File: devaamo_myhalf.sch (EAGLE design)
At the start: 18 parts, among them X1 PIIKKIRIMA-10

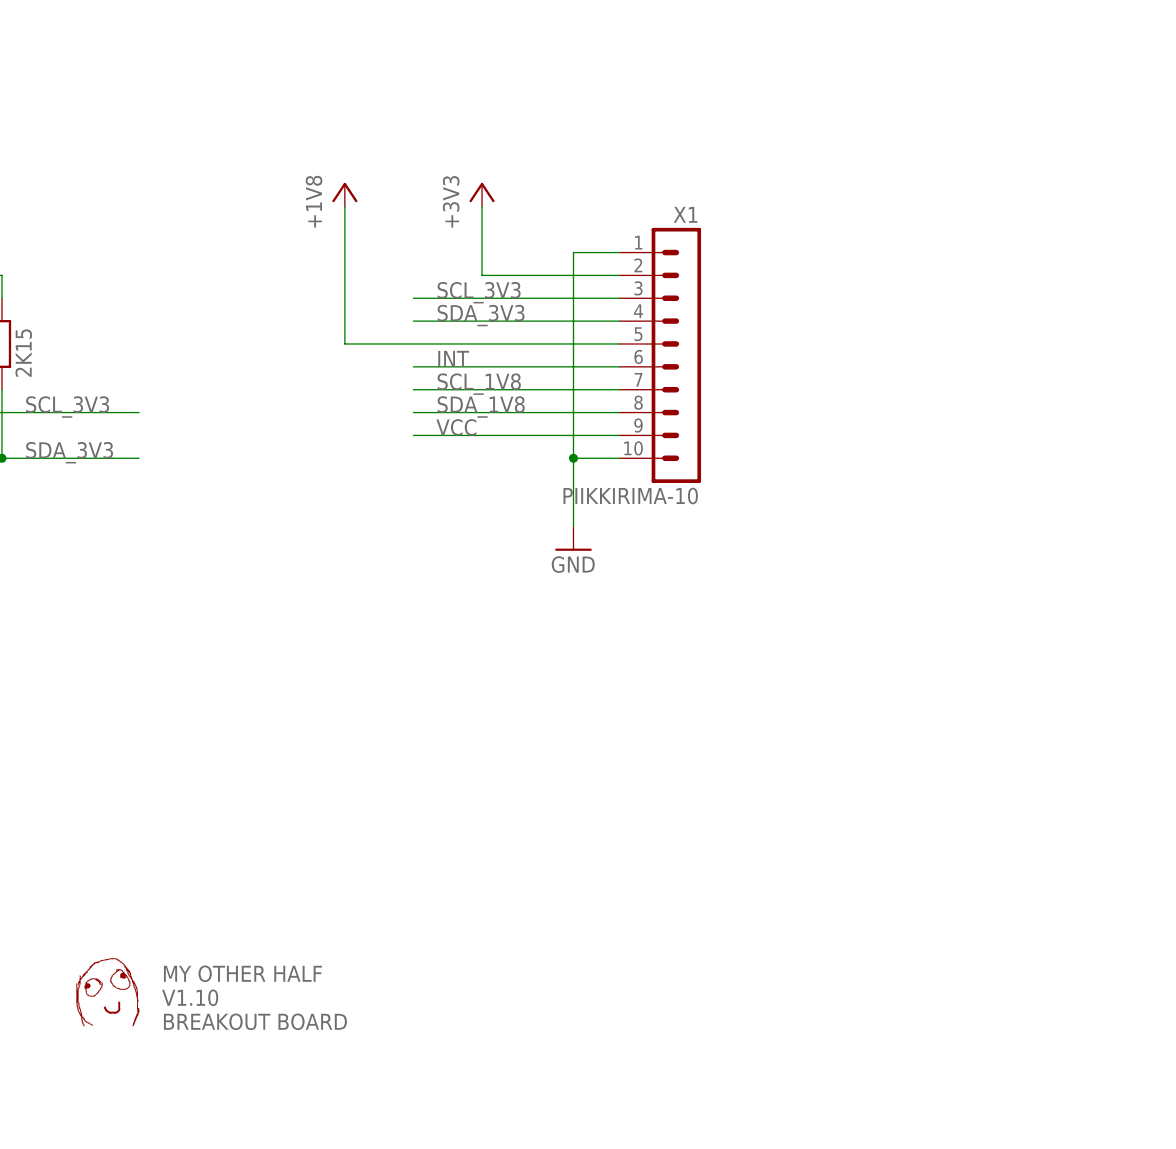
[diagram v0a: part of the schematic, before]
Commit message: smd connector add, relocate flash hole, resize pogopads to 2mm
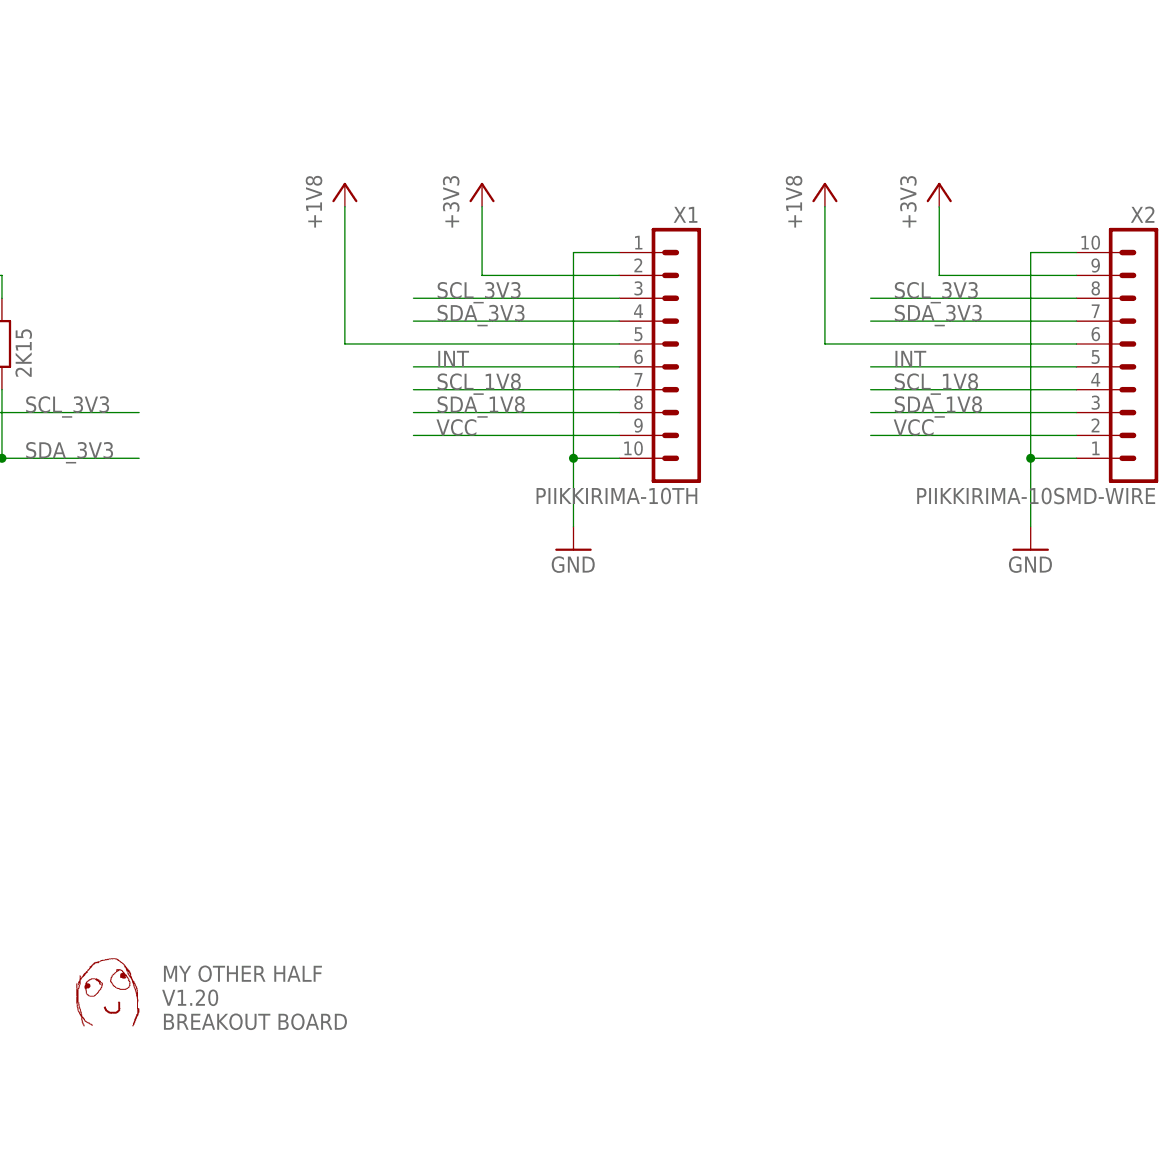
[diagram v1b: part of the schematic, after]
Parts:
- added X2: PIIKKIRIMA-10SMD-WIRE, OMAT_IC:PIIKKIRIMA-10SMD-WIRE
- X1: value PIIKKIRIMA-10 -> PIIKKIRIMA-10TH; device OMAT_IC:PIIKKIRIMA-10 -> OMAT_IC:PIIKKIRIMA-10TH
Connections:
- net +1V8: now also X2.5
- net +3V3: now also X2.2
- net GND: now also X2.1, X2.10
- net INT: now also X2.6
- net SCL_1V8: now also X2.7
- net SCL_3V3: now also X2.3
- net SDA_1V8: now also X2.8
- net SDA_3V3: now also X2.4
- net VCC: now also X2.9
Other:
- note added: "MY OTHER HALF V1.20 BREAKOUT BOARD"
- note removed: "MY OTHER HALF V1.10 BREAKOUT BOARD"
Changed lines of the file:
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@@
 <?xml version="1.0" encoding="utf-8"?>
 <!DOCTYPE eagle SYSTEM "eagle.dtd">
-<eagle version="6.4">
+<eagle version="6.5.0">
 <drawing>
 <settings>
@@
 <part name="+3V5" library="supply1" deviceset="+3V3" device=""/>
 <part name="GND7" library="supply1" deviceset="GND" device=""/>
-<part name="X1" library="OMAT_IC" deviceset="PIIKKIRIMA-10" device=""/>
+<part name="X1" library="OMAT_IC" deviceset="PIIKKIRIMA-10" device="TH"/>
 <part name="GND8" library="supply1" deviceset="GND" device=""/>
 <part name="+3V6" library="supply1" deviceset="+3V3" device=""/>
 <part name="+1V5" library="supply1" deviceset="+1V8" device=""/>
 <part name="U$3" library="oma" deviceset="DEVAAMO" device=""/>
+<part name="X2" library="OMAT_IC" deviceset="PIIKKIRIMA-10" device="SMD-WIRE"/>
+<part name="GND6" library="supply1" deviceset="GND" device=""/>
+<part name="+3V4" library="supply1" deviceset="+3V3" device=""/>
+<part name="+1V4" library="supply1" deviceset="+1V8" device=""/>
 </parts>
 <sheets>
@@
 <plain>
 <text x="259.08" y="-25.4" size="1.778" layer="95">MY OTHER HALF
-V1.10
+V1.20
 BREAKOUT BOARD</text>
 <text x="43.18" y="88.9" size="1.778" layer="95">CONNECTION TO JOLLA</text>
@@
 <instance part="+1V5" gate="G$1" x="279.4" y="66.04"/>
 <instance part="U$3" gate="G$1" x="88.9" y="104.14"/>
+<instance part="X2" gate="G$1" x="365.76" y="50.8" rot="MR0"/>
+<instance part="GND6" gate="1" x="355.6" y="27.94"/>
+<instance part="+3V4" gate="G$1" x="345.44" y="68.58"/>
+<instance part="+1V4" gate="G$1" x="332.74" y="66.04"/>
 </instances>
 <busses>
@@
 <label x="289.56" y="48.26" size="1.778" layer="95"/>
 </segment>
+<segment>
+<wire x1="360.68" y1="48.26" x2="337.82" y2="48.26" width="0.1524" layer="91"/>
+<label x="340.36" y="48.26" size="1.778" layer="95"/>
+<pinref part="X2" gate="G$1" pin="6"/>
+</segment>
 </net>
 <net name="SDA_1V8" class="0">
@@
 <label x="289.56" y="43.18" size="1.778" layer="95"/>
 </segment>
+<segment>
+<wire x1="360.68" y1="43.18" x2="337.82" y2="43.18" width="0.1524" layer="91"/>
+<label x="340.36" y="43.18" size="1.778" layer="95"/>
+<pinref part="X2" gate="G$1" pin="8"/>
+</segment>
 </net>
 <net name="SCL_1V8" class="0">
@@
 <label x="289.56" y="45.72" size="1.778" layer="95"/>
 </segment>
+<segment>
+<wire x1="360.68" y1="45.72" x2="337.82" y2="45.72" width="0.1524" layer="91"/>
+<label x="340.36" y="45.72" size="1.778" layer="95"/>
+<pinref part="X2" gate="G$1" pin="7"/>
+</segment>
 </net>
 <net name="VCC" class="0">
@@
 <wire x1="309.88" y1="40.64" x2="287.02" y2="40.64" width="0.1524" layer="91"/>
 <label x="289.56" y="40.64" size="1.778" layer="95"/>
+</segment>
+<segment>
+<wire x1="360.68" y1="40.64" x2="337.82" y2="40.64" width="0.1524" layer="91"/>
+<label x="340.36" y="40.64" size="1.778" layer="95"/>
+<pinref part="X2" gate="G$1" pin="9"/>
 </segment>
 </net>
@@
 <junction x="304.8" y="38.1"/>
 </segment>
+<segment>
+<wire x1="360.68" y1="38.1" x2="355.6" y2="38.1" width="0.1524" layer="91"/>
+<wire x1="355.6" y1="38.1" x2="355.6" y2="30.48" width="0.1524" layer="91"/>
+<pinref part="GND6" gate="1" pin="GND"/>
+<wire x1="360.68" y1="60.96" x2="355.6" y2="60.96" width="0.1524" layer="91"/>
+<wire x1="355.6" y1="60.96" x2="355.6" y2="38.1" width="0.1524" layer="91"/>
+<junction x="355.6" y="38.1"/>
+<pinref part="X2" gate="G$1" pin="10"/>
+<pinref part="X2" gate="G$1" pin="1"/>
+</segment>
 </net>
 <net name="+1V8" class="0">
@@
 <pinref part="X1" gate="G$1" pin="5"/>
 <wire x1="279.4" y1="50.8" x2="309.88" y2="50.8" width="0.1524" layer="91"/>
+</segment>
+<segment>
+<pinref part="+1V4" gate="G$1" pin="+1V8"/>
+<wire x1="332.74" y1="50.8" x2="332.74" y2="66.04" width="0.1524" layer="91"/>
+<wire x1="332.74" y1="50.8" x2="360.68" y2="50.8" width="0.1524" layer="91"/>
+<pinref part="X2" gate="G$1" pin="5"/>
 </segment>
 </net>
@@
 <wire x1="294.64" y1="66.04" x2="294.64" y2="58.42" width="0.1524" layer="91"/>
 </segment>
+<segment>
+<wire x1="360.68" y1="58.42" x2="345.44" y2="58.42" width="0.1524" layer="91"/>
+<pinref part="+3V4" gate="G$1" pin="+3V3"/>
+<wire x1="345.44" y1="66.04" x2="345.44" y2="58.42" width="0.1524" layer="91"/>
+<pinref part="X2" gate="G$1" pin="2"/>
+</segment>
 </net>
 <net name="SCL_3V3" class="0">
@@
 <label x="289.56" y="55.88" size="1.778" layer="95"/>
 </segment>
+<segment>
+<wire x1="360.68" y1="55.88" x2="337.82" y2="55.88" width="0.1524" layer="91"/>
+<label x="340.36" y="55.88" size="1.778" layer="95"/>
+<pinref part="X2" gate="G$1" pin="3"/>
+</segment>
 </net>
 <net name="SDA_3V3" class="0">
@@
 <label x="289.56" y="53.34" size="1.778" layer="95"/>
 </segment>
-</net>
+<segment>
+<wire x1="360.68" y1="53.34" x2="337.82" y2="53.34" width="0.1524" layer="91"/>
+<label x="340.36" y="53.34" size="1.778" layer="95"/>
+<pinref part="X2" gate="G$1" pin="4"/>
+</segment>
+</net>

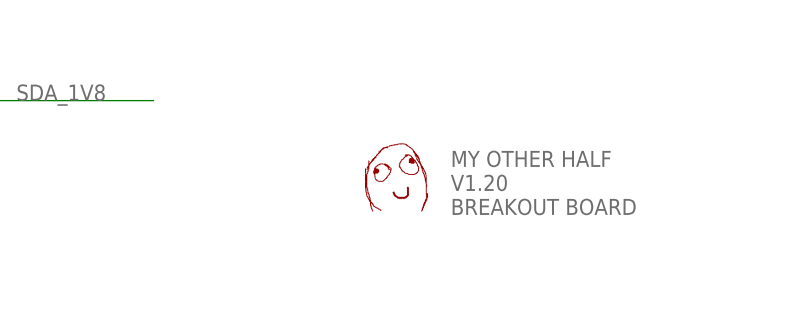
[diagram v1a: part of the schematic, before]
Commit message: oshw logo added
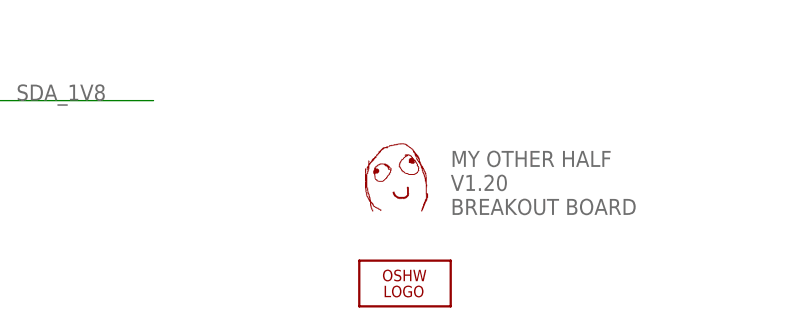
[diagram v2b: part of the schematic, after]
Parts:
- added LOGO1: OSHW_LOGO_FILLX0200-NT, ohw-logo:OSHW_LOGO_FILLX0200-NT
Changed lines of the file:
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@@
 <part name="+3V4" library="supply1" deviceset="+3V3" device=""/>
 <part name="+1V4" library="supply1" deviceset="+1V8" device=""/>
+<part name="LOGO1" library="ohw-logo" deviceset="OSHW_LOGO_FILL" device="X0200-NT"/>
 </parts>
 <sheets>
@@
 <instance part="+3V4" gate="G$1" x="345.44" y="68.58"/>
 <instance part="+1V4" gate="G$1" x="332.74" y="66.04"/>
+<instance part="LOGO1" gate="G$1" x="254" y="-33.02"/>
 </instances>
 <busses>
